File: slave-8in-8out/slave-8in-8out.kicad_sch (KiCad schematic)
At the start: 47 parts, among them J1 Conn_01x06_Male, J2 Screw_Terminal_01x02, J3 Conn_01x06_Female, J4 Screw_Terminal_01x04, J5 Screw_Terminal_01x04, J6 Screw_Terminal_01x04, J7 Screw_Terminal_01x04, J8 Conn_01x10_Female, J9 Screw_Terminal_01x02, SW1 SW_DIP_x03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

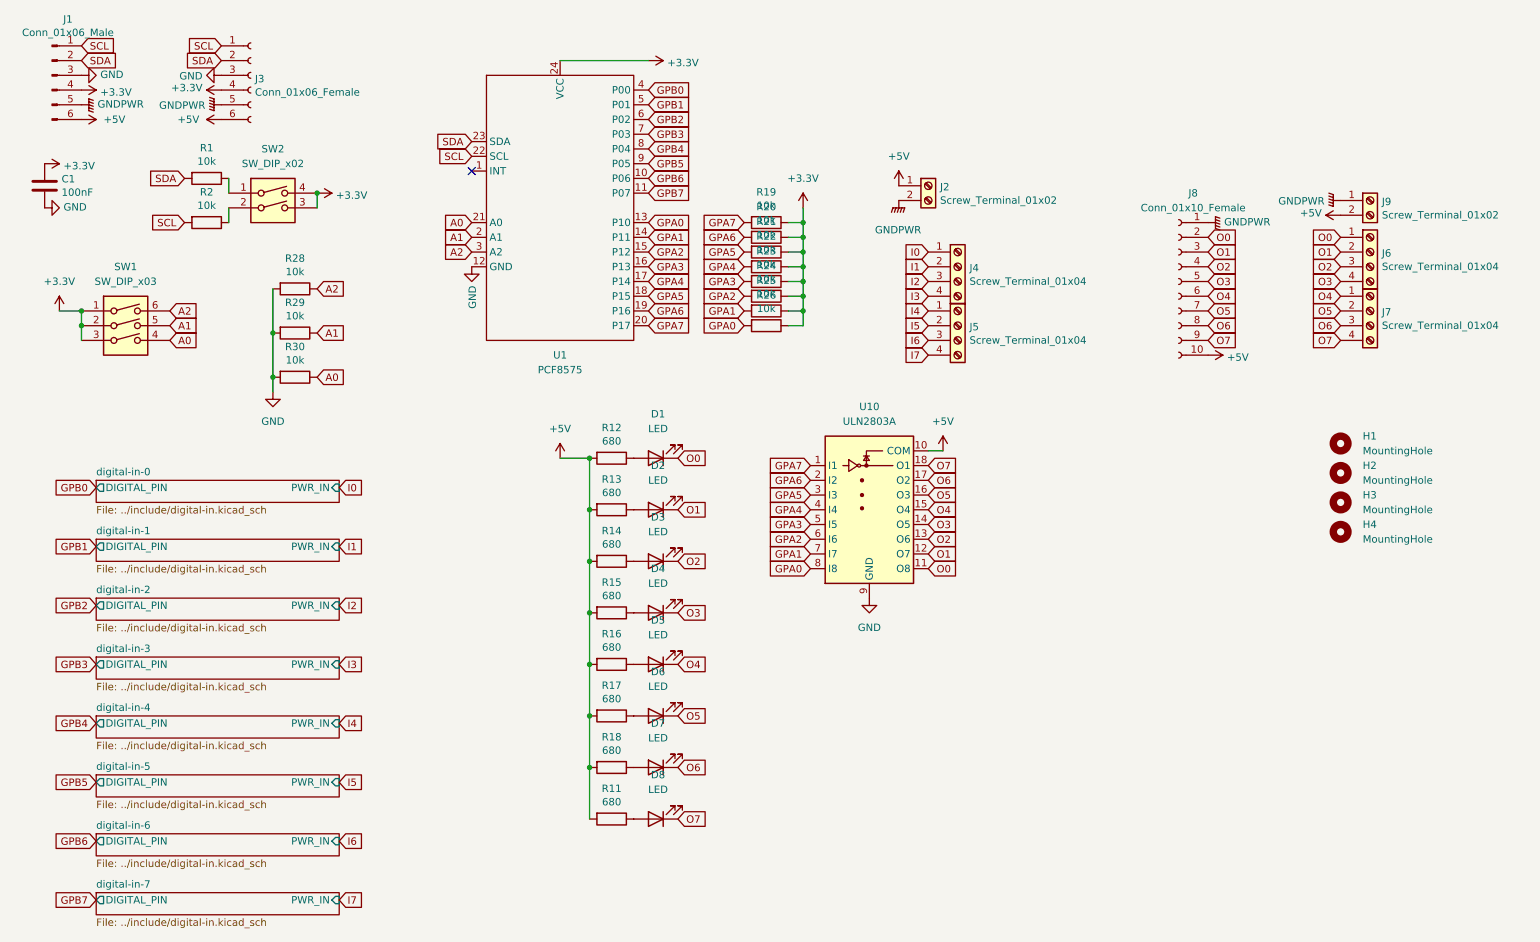
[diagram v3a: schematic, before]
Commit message: update slave-8in-8out labels
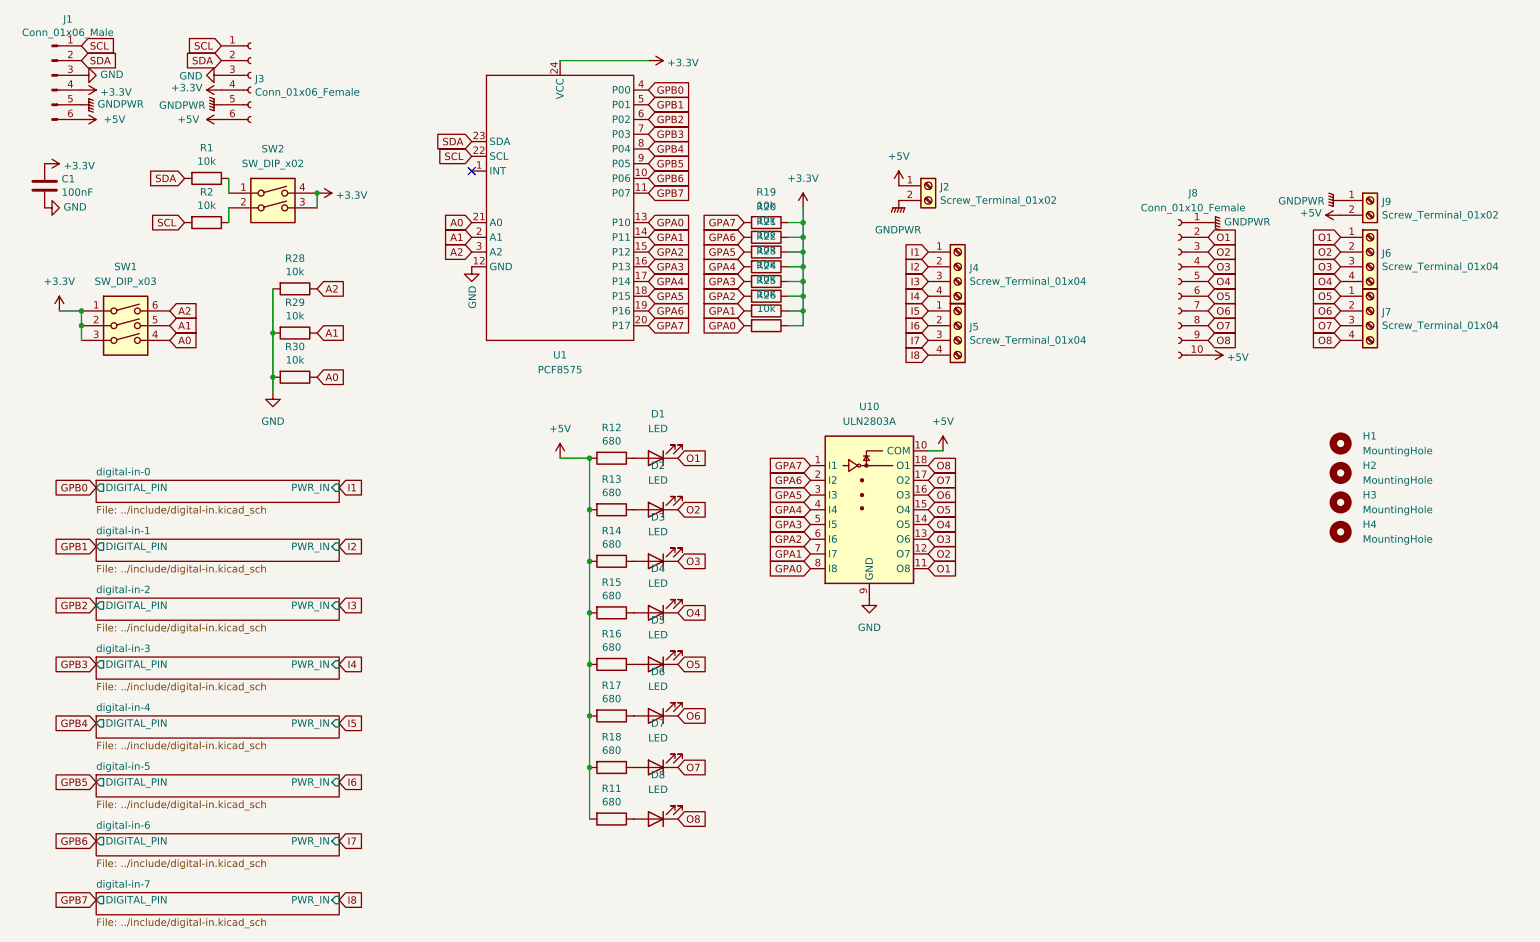
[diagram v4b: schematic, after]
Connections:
- net I0 is gone; now on net I1: J4.1 (Pin_1)
- net O0 is gone; now on net O1: D1.1 (K), J6.1 (Pin_1), J8.2 (Pin_2), U10.11 (O8)
- net I1: no longer J4.2 (Pin_2)
- net I2: now also J4.2 (Pin_2); no longer J4.3 (Pin_3)
- net I3: now also J4.3 (Pin_3); no longer J4.4 (Pin_4)
- net I4: now also J4.4 (Pin_4); no longer J5.1 (Pin_1)
- net I5: now also J5.1 (Pin_1); no longer J5.2 (Pin_2)
- net I6: now also J5.2 (Pin_2); no longer J5.3 (Pin_3)
- net I7: now also J5.3 (Pin_3); no longer J5.4 (Pin_4)
- net O1: no longer D2.1 (K), J6.2 (Pin_2), J8.3 (Pin_3), U10.12 (O7)
- net O2: now also D2.1 (K), J6.2 (Pin_2), J8.3 (Pin_3), U10.12 (O7); no longer D3.1 (K), J6.3 (Pin_3), J8.4 (Pin_4), U10.13 (O6)
- net O3: now also D3.1 (K), J6.3 (Pin_3), J8.4 (Pin_4), U10.13 (O6); no longer D4.1 (K), J6.4 (Pin_4), J8.5 (Pin_5), U10.14 (O5)
- net O4: now also D4.1 (K), J6.4 (Pin_4), J8.5 (Pin_5), U10.14 (O5); no longer D5.1 (K), J7.1 (Pin_1), J8.6 (Pin_6), U10.15 (O4)
- net O5: now also D5.1 (K), J7.1 (Pin_1), J8.6 (Pin_6), U10.15 (O4); no longer D6.1 (K), J7.2 (Pin_2), J8.7 (Pin_7), U10.16 (O3)
- net O6: now also D6.1 (K), J7.2 (Pin_2), J8.7 (Pin_7), U10.16 (O3); no longer D7.1 (K), J7.3 (Pin_3), J8.8 (Pin_8), U10.17 (O2)
- net O7: now also D7.1 (K), J7.3 (Pin_3), J8.8 (Pin_8), U10.17 (O2); no longer D8.1 (K), J7.4 (Pin_4), J8.9 (Pin_9), U10.18 (O1)
- new net I8: J5.4 (Pin_4)
- new net O8: D8.1 (K), J7.4 (Pin_4), J8.9 (Pin_9), U10.18 (O1)

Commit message: update slave-8in-8out
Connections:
- net +5V: now also J2.2 (Pin_2)
- net GNDPWR: no longer J2.2 (Pin_2)
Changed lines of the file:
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@@
   (junction (at 152.4 64.77) (diameter 0) (color 0 0 0 0))
   (junction (at 152.4 67.31) (diameter 0) (color 0 0 0 0))
+  (junction (at 168.91 45.72) (diameter 0) (color 0 0 0 0))
   (no_connect (at 95.25 43.18))
   (wire (pts (xy 24.13 67.31) (xy 27.94 67.31))
@@
     (stroke (width 0) (type default) (color 0 0 0 0))
   )
+  (wire (pts (xy 168.91 45.72) (xy 168.91 48.26))
+    (stroke (width 0) (type default) (color 0 0 0 0))
+  )
   (wire (pts (xy 173.99 91.44) (xy 176.53 91.44))
     (stroke (width 0) (type solid) (color 0 0 0 0))
@@
     )
     (property "Datasheet" "" (id 3) (at 50.8 31.75 0)
-      (effects (font (size 1.27 1.27)) hide)
-    )
-    (pin "1")
-  )
-  (symbol (lib_id "power:GNDPWR") (at 168.91 48.26 0) (unit 1)
-    (in_bom yes) (on_board yes) (fields_autoplaced)
-    (property "Reference" "#PWR0142" (id 0) (at 168.91 53.34 0)
-      (effects (font (size 1.27 1.27)) hide)
-    )
-    (property "Value" "GNDPWR" (id 1) (at 168.783 53.34 0))
-    (property "Footprint" "" (id 2) (at 168.91 49.53 0)
-      (effects (font (size 1.27 1.27)) hide)
-    )
-    (property "Datasheet" "" (id 3) (at 168.91 49.53 0)
       (effects (font (size 1.27 1.27)) hide)
     )
@@
       (reference "#PWR0141") (unit 1) (value "+3.3V") (footprint "")
     )
-    (path "/d85541cb-1b2b-4244-b900-51571a4724ac"
-      (reference "#PWR0142") (unit 1) (value "GNDPWR") (footprint "")
-    )
     (path "/00000000-0000-0000-0000-000060167899"
